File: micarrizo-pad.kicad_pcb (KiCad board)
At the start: 2 copper layers, 128.6 x 81.8 mm, 20 parts, among them U1 The-Big-Switch, U2 KB2040

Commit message: finish pcb
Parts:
- moved S1 6.20 mm to (134.9, 65.1)
- moved U1 5.32 mm to (60.3, 84.9)
- moved MX2 5.32 mm to (121.4, 65.9)
- moved D2 5.32 mm to (129.4, 65.9)
- moved D5 5.32 mm to (148.4, 84.9)
- moved MX5 5.32 mm to (140.5, 84.9)
- moved D1 4.76 mm to (110.3, 65.9)
- moved MX1 4.76 mm to (102.4, 65.9)
- moved D9 4.76 mm to (148.4, 104.0)
- moved MX8 4.76 mm to (140.5, 104.0)
- moved MX4 3.37 mm to (121.4, 84.9)
- moved D4 3.37 mm to (129.4, 84.9)
- moved D3 2.38 mm to (110.3, 84.9)
- moved MX7 2.38 mm to (121.4, 104.0)
- moved D8 2.38 mm to (129.4, 104.0)
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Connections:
- U2 pad 10: COL1 -> COL0
- U2 pad 11: COL2 -> COL1
- U2 pad 12: COL3 -> COL2
- U2 pad 13: COL4 -> COL3
- U2 pad 20: ENC_A -> Net-(U2-Pad20)
- U2 pad 21: ENC_B -> Net-(U2-Pad21)
- U2 pad 22: ENC_SW -> Net-(U2-Pad22)
- U2 pad 24: Net-(U2-Pad24) -> ENC_A
- U2 pad 25: Net-(U2-Pad25) -> ENC_B
- U2 pad 26: Net-(U2-Pad26) -> ENC_SW
- U2 pad 7: ROW1 -> ROW2
- U2 pad 8: ROW2 -> ROW1
- U2 pad 9: ROW3 -> ROW0
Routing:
- net ROW2: track 0.00 -> 161.6 mm
- net ROW1: track 0.00 -> 128.0 mm
- net COL3: track 0.00 -> 123.9 mm
- net ENC_B: track 0.00 -> 110.1 mm
- net ENC_A: track 0.00 -> 108.8 mm
- net COL2: track 0.00 -> 102.7 mm
- net ROW0: track 0.00 -> 94.1 mm
- net COL1: track 0.00 -> 87.0 mm
- net ENC_SW: track 0.00 -> 85.2 mm
- net Net-(D6-Pad2): track 0.00 -> 41.5 mm
- net COL0: track 0.00 -> 27.0 mm
- net Net-(S1-Pad3): track 0.00 -> 11.4 mm
- net Net-(D2-Pad2): track 0.00 -> 6.62 mm
- net Net-(D1-Pad2): track 0.00 -> 6.62 mm
- net Net-(D9-Pad2): track 0.00 -> 6.62 mm
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- added copper zone on B.Cu, net GND
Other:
- board size 128.6 x 81.8 mm -> 120.7 x 81.8 mm

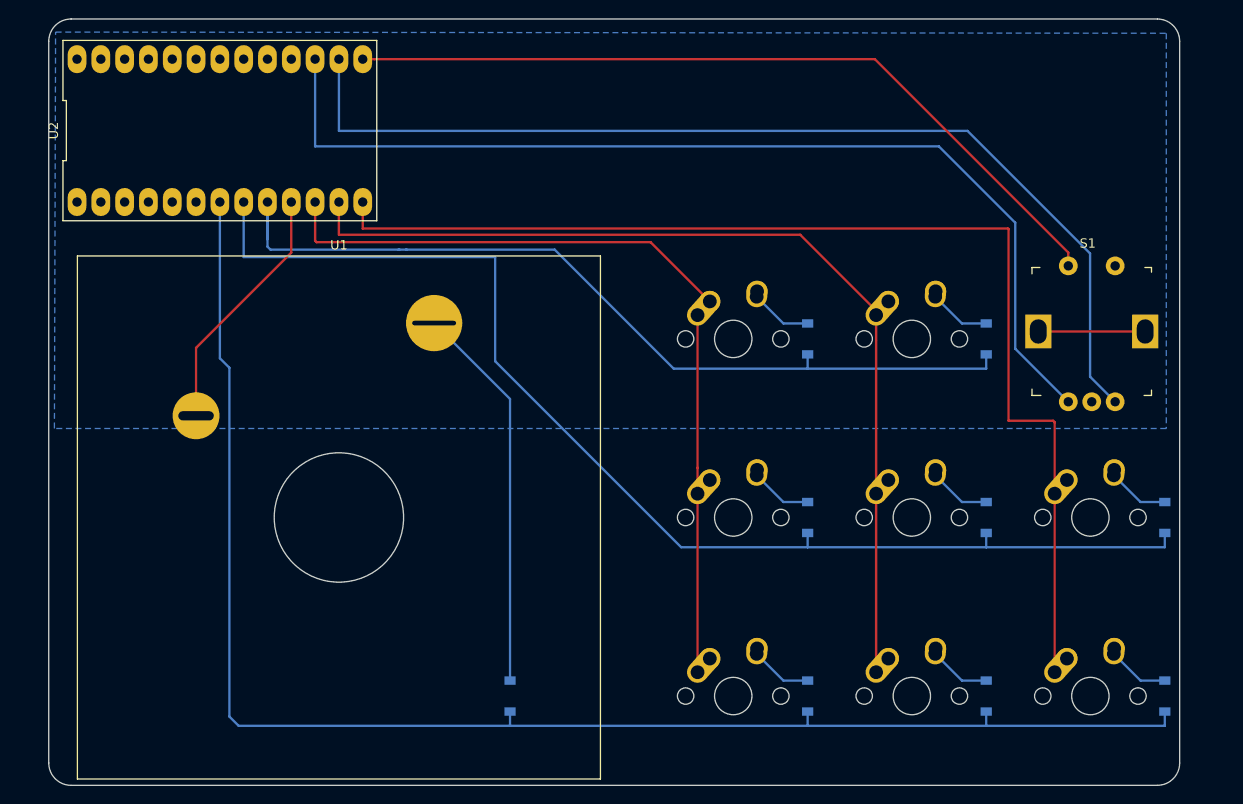
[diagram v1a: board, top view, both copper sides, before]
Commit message: complete pcb add text
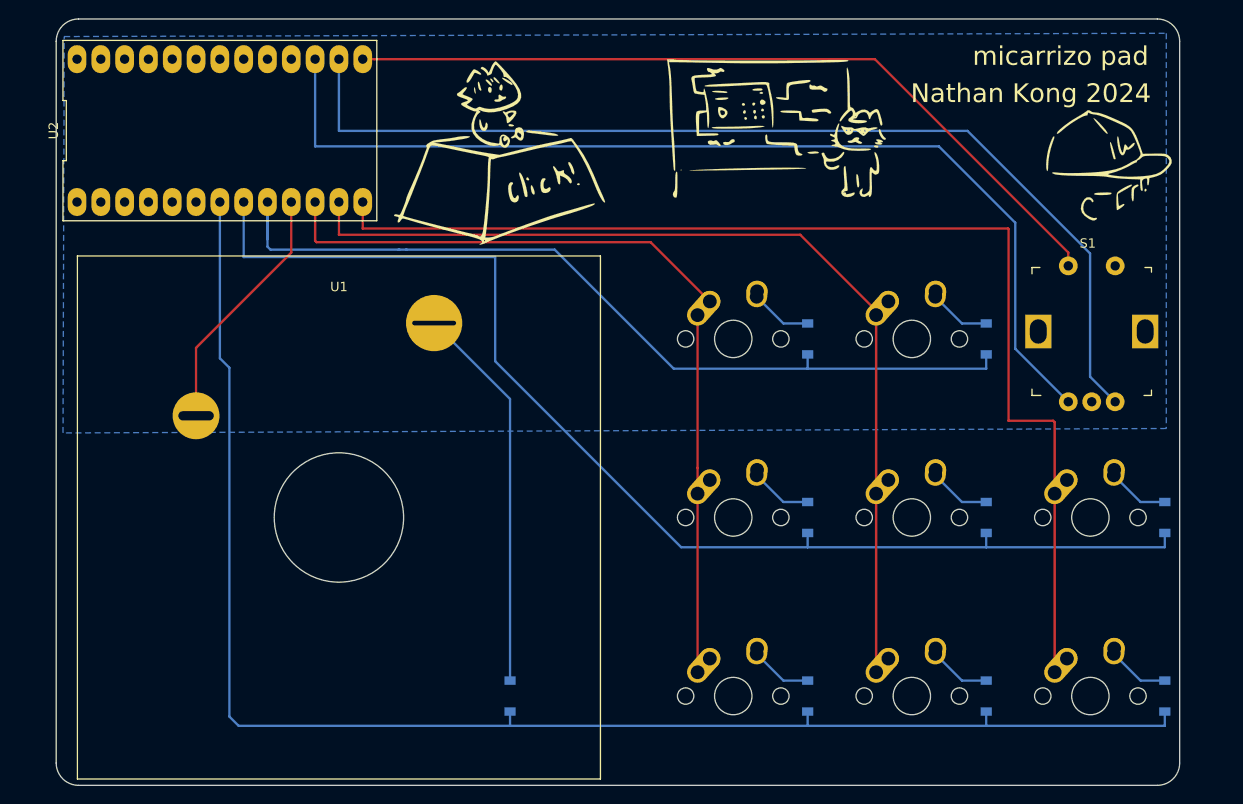
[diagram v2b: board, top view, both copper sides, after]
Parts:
- added G***: LOGO, The Big Switch:meow, F.Cu at (93.7, 45.2)
- added G***: LOGO, The Big Switch:icon, F.Cu at (142.1, 48.4)
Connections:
- S1 pad 3: Net-(S1-Pad3) -> (no net)
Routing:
- net Net-(S1-Pad3): track 11.4 -> 0.00 mm
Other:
- board size 120.7 x 81.8 mm -> 119.9 x 81.8 mm
- board text added: "Nathan Kong 2024"
- board text added: "micarrizo pad"
